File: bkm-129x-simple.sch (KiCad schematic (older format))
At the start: 52 parts, among them J1 YG1, J2 PBB1, J3 PRR1, J4 SYNC1, J5 Conn_02x32_Row_Letter_Last, Q1 DTC144EKA, U1 ADG1611, U2 THS7374, U3 arduino-nano-v3, U4 74LVC125, U5 MIC3940

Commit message: Fixed MIC3940 -> MIC3490
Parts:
- removed U5: MIC3940, TO_SOT_Packages_SMD:SOT-23-5_HandSoldering, symbol MIC3940
- added U5: MIC3490-3.3, TO_SOT_Packages_SMD:SOT-23-5_HandSoldering, symbol MIC3490
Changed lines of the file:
@@
 LIBS:adg1611
 LIBS:dtc144eka
-LIBS:mic3940
+LIBS:mic3490
 LIBS:bkm-129x-simple-cache
 EELAYER 25 0
@@
 Wire Wire Line
 	7350 4100 7400 4100
-$Comp
-L MIC3940 U5
-U 1 1 5E374B80
-P 5250 1200
-F 0 "U5" H 5250 1450 60  0000 C CNN
-F 1 "MIC3940" H 5250 950 60  0000 C CNN
-F 2 "TO_SOT_Packages_SMD:SOT-23-5_HandSoldering" H 5050 1200 60  0001 C CNN
-F 3 "" H 5050 1200 60  0001 C CNN
-	1    5250 1200
-	1    0    0    -1
-$EndComp
 Wire Wire Line
 	4800 1350 4750 1350
@@
 Text Label 3050 4900 3    60   ~ 0
 MCU_SCK
+$Comp
+L MIC3490 U5
+U 1 1 5E4D822E
+P 5250 1200
+F 0 "U5" H 5250 1450 60  0000 C CNN
+F 1 "MIC3490-3.3" H 5250 950 60  0000 C CNN
+F 2 "TO_SOT_Packages_SMD:SOT-23-5_HandSoldering" H 5050 1200 60  0001 C CNN
+F 3 "" H 5050 1200 60  0001 C CNN
+	1    5250 1200
+	1    0    0    -1
+$EndComp
 $EndSCHEMATC

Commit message: Added revision, compatibility and credits
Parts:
- R9: value 150R -> 0R
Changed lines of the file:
@@
 P 6700 2650
 F 0 "R9" V 6780 2650 50  0000 C CNN
-F 1 "150R" V 6700 2650 50  0000 C CNN
+F 1 "0R" V 6700 2650 50  0000 C CNN
 F 2 "Resistors_SMD:R_0805_HandSoldering" V 6630 2650 50  0001 C CNN
 F 3 "" H 6700 2650 50  0001 C CNN

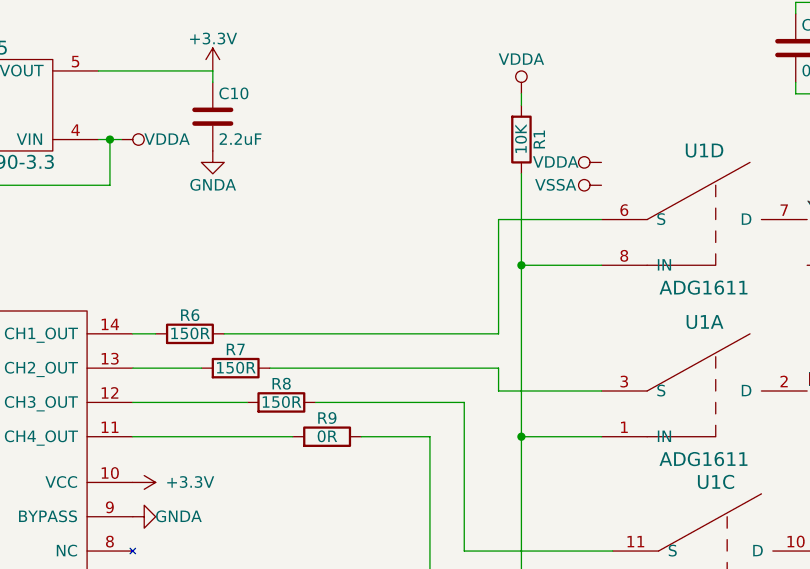
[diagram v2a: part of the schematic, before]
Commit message: Added overbrightness fix
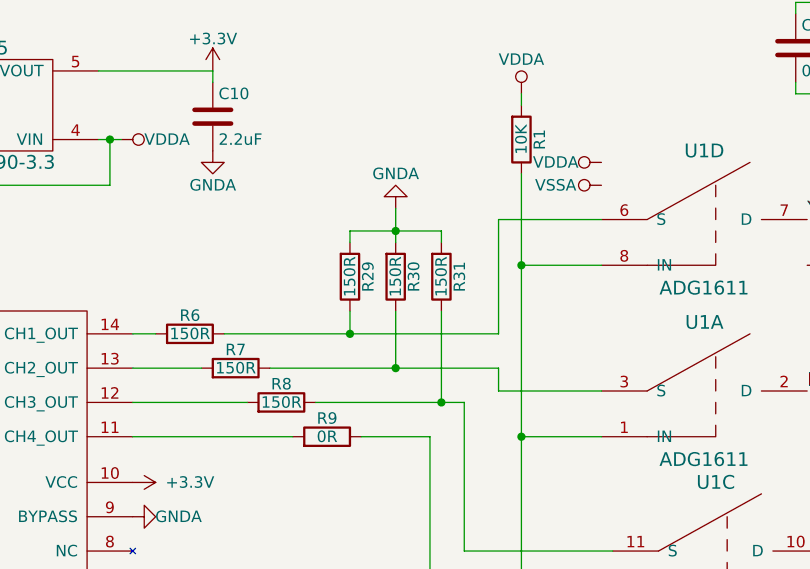
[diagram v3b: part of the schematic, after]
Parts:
- added R29, R30, R31: 150R, Resistors_SMD:R_0805_HandSoldering, symbol R
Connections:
- net GND: now also R29.2, R30.2, R31.2
- net at R6.1, U1.6 (S): now also R29.1
- net at R7.1, U1.3 (S): now also R30.1
- net at R8.1, U1.11 (S): now also R31.1

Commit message: Rev. D: THS7374 LPF, Kicad 5
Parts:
- C1, C10, C11, C12, C2, C3, C4, C5, C6, C9: symbol C -> bkm-129x-simple-rescue:C
- C13, C7, C8: symbol CP -> bkm-129x-simple-rescue:CP
- J1, J2, J3, J4: symbol Conn_Coaxial -> bkm-129x-simple-rescue:Conn_Coaxial
- J5: symbol Conn_02x32_Row_Letter_Last -> bkm-129x-simple-rescue:Conn_02x32_Row_Letter_Last
- Q1: symbol DTC144EKA -> dtc144eka:DTC144EKA
- R1, R10, R11, R12, R13, R14, R15, R16, R17, R18, R19, R2, R20, R21, R22, R23, R24, R25, R26, R27, R28, R29, R3, R30, R31, R4, R5, R6, R7, R8, R9: symbol R -> bkm-129x-simple-rescue:R
- U1: symbol ADG1611 -> adg1611:ADG1611
- U2: symbol THS7374 -> ths7374:THS7374
- U3: symbol arduino-nano-v3 -> arduino-nano-v3:arduino-nano-v3
- U4: symbol 74LVC125 -> bkm-129x-simple-rescue:74LVC125
- U5: symbol MIC3490 -> mic3490:MIC3490
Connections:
- net +3V3: now also U2.9 (BYPASS)
- net GND: no longer U2.9 (BYPASS)
